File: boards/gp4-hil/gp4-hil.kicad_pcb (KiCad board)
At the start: 4 copper layers, 145 x 41 mm, 488 parts, among them J1 BEL_FUSE_0826-1G1T-23-F, J2 XILINX_JTAG, J3 XILINX_JTAG_ICESIDE, J4 XILINX_JTAG_ICESIDE, K1 CONN_3_PWROUT, P1 GPAK_ZIF, P2 2x10 HEADER, Q1 SSM6N58NU, Q11 SSM6N58NU, Q12 DMP2069UFY4, Q13 SSM6N58NU, Q14 SSM6N58NU, Q15 SSM6N58NU, Q16 SSM6N58NU, Q17 SSM6N58NU, Q18 SSM6N58NU, Q19 SSM6N58NU, Q20 SSM6N58NU, Q21 SSM6N58NU, Q22 DMP2069UFY4, U1 MIC2288-DFN, U10 AD9609, U11 DAC084S085, U12 DAC084S085, U13 DAC084S085, U14 DAC084S085, U15 TS3A4751, U16 TS3A4751, U17 TS3A4751, U18 TS3A4751, U19 TS3A4751, U2 XC7A100T-1FTG256C, U20 SIP32408, U21 SIP32408, U22 SIP32408, U23 SIP32408, U24 SIP32408, U25 TS3A4751, U26 TS3A4751, U27 TS3A4751, U28 TS3A4751, U29 TXB0104RUT, U3 LTC3374-QFN, U30 TXB0104RUT, U31 ADA4937-2, U32 SIP32408, U33 125 MHz, U34 INA199A2RSW, U35 INA199A2RSW, U36 INA199A2RSW, U4 SIP32408, U5 KSZ9031RN, U6 W25Q32FW, U7 25 MHz, U8 ADG726, U9 AD9609

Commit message: More JTAG/config stuff
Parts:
- C163, C164, C165, C166, C182, C24, R121, R124, R127, R128, R130, R131, R132, R135, R136, R137: moved to B.Cu
- TP22, TP23: footprint azonenberg_pcb:TESTPOINT_SMT_KEYSTONE_5016 -> azonenberg_pcb:TESTPOINT_SMT_0.5MM
- moved TP35 126.6 mm to (148.3, 111.0)
- moved R122 123.5 mm to (142.3, 97.0), turned to 270 degrees
- moved R123 122.3 mm to (143.7, 96.9), turned to 270 degrees
- moved R132 122.2 mm to (143.7, 97.0), turned to 270 degrees
- moved R130 113.2 mm to (138.3, 95.2)
- moved R134 113.1 mm to (145.5, 87.8), turned to 180 degrees
- moved C143 112.1 mm to (138.7, 92.3), turned to 90 degrees
- moved R133 110.7 mm to (142.3, 87.2), turned to 270 degrees
- moved U6 106.0 mm to (143.0, 92.2)
- moved R127 104.8 mm to (125.0, 97.2), turned to 180 degrees
- moved R128 102.6 mm to (125.0, 96.2), turned to 180 degrees
- moved R121 101.7 mm to (112.5, 107.7), turned to 270 degrees
- moved R125 99.3 mm to (125.8, 98.1), turned to 180 degrees
- moved R129 95.8 mm to (143.7, 87.2), turned to 90 degrees
- moved R131 94.7 mm to (142.3, 87.2), turned to 90 degrees
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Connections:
- U2 pad N9: /Ethernet + JTAG/VPP_EN -> /Ethernet + JTAG/JTAGA_OE
- U2 pad P6: /Ethernet + JTAG/JTAGB_OE -> /Ethernet + JTAG/VPP_EN
- U2 pad R10: /DUT/DUT_VDD2_EN -> /Ethernet + JTAG/JTAGA_TDO
- U2 pad R11: /Ethernet + JTAG/VDD1_3V3_EN -> /Ethernet + JTAG/JTAGA_TMS
- U2 pad R5: /Ethernet + JTAG/JTAGB_TMS -> /DUT/DUT_VDD2_EN
- U2 pad R6: /Ethernet + JTAG/JTAGB_TDO -> /Ethernet + JTAG/JTAGB_TDI
- U2 pad R7: /Ethernet + JTAG/JTAGB_TDI -> /Ethernet + JTAG/JTAGB_TCK
- U2 pad R8: /Ethernet + JTAG/JTAGA_TMS -> /Ethernet + JTAG/JTAGB_OE
- U2 pad T10: /Ethernet + JTAG/JTAGA_OE -> /Ethernet + JTAG/JTAGA_TCK
- U2 pad T5: /Ethernet + JTAG/JTAGB_TCK -> /Ethernet + JTAG/VDD1_3V3_EN
- U2 pad T7: /Ethernet + JTAG/JTAGA_TCK -> /Ethernet + JTAG/JTAGB_TDO
- U2 pad T8: /Ethernet + JTAG/JTAGA_TDO -> /Ethernet + JTAG/JTAGB_TMS
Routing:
- net /Analog IO/GND: track 328.0 -> 571.1 mm, vias 79 -> 95
- net /Analog IO/1V8: track 81.6 -> 191.3 mm, vias 18 -> 29
- net /FPGA support/JTAG_TMS: track 0.71 -> 57.6 mm
- net /FPGA support/JTAG_TCK: track 0.71 -> 55.9 mm, vias 1 -> 2
- net /FPGA support/JTAG_TDI: track 0.71 -> 52.3 mm, vias 1 -> 2
- net /FPGA support/JTAG_TDO: track 0.00 -> 47.3 mm
- net /FPGA support/FLASH_SCK: track 0.71 -> 42.9 mm, vias 1 -> 2
- net /FPGA support/FLASH_DQ3T: track 0.00 -> 31.1 mm, vias 0 -> 2
- net /FPGA support/FLASH_DQ0T: track 0.00 -> 26.6 mm, vias 0 -> 1
- net /FPGA support/FLASH_DQ2T: track 0.00 -> 18.4 mm
- net /FPGA support/FLASH_CS_NT: track 0.00 -> 18.2 mm, vias 0 -> 1
- net /FPGA support/FLASH_DQ1T: track 0.00 -> 17.4 mm, vias 0 -> 1
- net /Ethernet + JTAG/JTAGB_VCCAUX: track 0.00 -> 17.0 mm, vias 0 -> 1
- net /Ethernet + JTAG/JTAGA_OE: track 0.00 -> 16.2 mm, vias 0 -> 2
- net /Ethernet + JTAG/JTAGB_OE: track 0.71 -> 16.1 mm, vias 1 -> 0
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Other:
- board size 145 x 41 mm -> 145 x 60 mm
- board text added: "5V DC"
- board text added: "FPGA JTAG"
- board text added: "FPGA config"
- board text added: "GND"
- board text added: "GreenPak Toolchain Test v0.1 A. Zonenberg / 2016-05-26"
- board text added: "MASTER JTAG A"
- board text added: "MASTER JTAG B"
- board text removed: "Clocks"
- board text removed: "FPGA config straps"
- board text removed: "FPGA config/boot"
- board text removed: "JTAG"
- board text removed: "Power inlet"

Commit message: Began routing level shifters
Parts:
- C116, C117, C118, C119, C120, C121, C123, C124, C140, C172, F1, L8, Q22, R103, R117, R118, R120, R177: moved to B.Cu
- moved TP36 148.7 mm to (53.3, 114.8)
- moved U23 145.8 mm to (97.8, 108.8), turned to 270 degrees
- moved Q1 143.9 mm to (140.7, 42.7), turned to 90 degrees
- moved R81 143.3 mm to (143.7, 41.6)
- moved U22 141.9 mm to (97.8, 105.5), turned to 270 degrees
- moved C140 138.7 mm to (97.9, 105.7), turned to 180 degrees
- moved C58 138.4 mm to (148.7, 44.1)
- moved C61 137.6 mm to (151.9, 44.0)
- moved C62 137.6 mm to (156.9, 44.2)
- moved D1 137.4 mm to (143.6, 44.2)
- moved C57 137.2 mm to (152.2, 41.4)
- moved C59 137.2 mm to (149.1, 41.5)
- moved C60 137.2 mm to (156.9, 41.6)
- moved R118 131.9 mm to (98.5, 107.7), turned to 90 degrees
- moved R117 126.3 mm to (100.0, 108.0), turned to 270 degrees
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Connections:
- U2 pad A2: /Digital IO/GPIO19_DEN -> (no net)
- U2 pad B2: /Digital IO/GPIO18_DEN -> (no net)
- U2 pad C1: /Digital IO/GPIO20_DEN -> (no net)
- U2 pad C2: /Digital IO/GPIO17_DEN -> (no net)
- U2 pad C3: /Digital IO/GPIO16_DEN -> (no net)
- U2 pad C6: /Digital IO/GPIO13_DEN -> (no net)
- U2 pad C7: /Digital IO/GPIO12_DEN -> (no net)
- U2 pad D5: /Digital IO/GPIO15_DEN -> (no net)
- U2 pad D6: /Digital IO/GPIO14_DEN -> (no net)
- U2 pad G11: (no net) -> /Analog IO/ADC_A_MODE
- U2 pad G15: (no net) -> /Analog IO/DAC_SCLK
- U2 pad J15: /Analog IO/DAC_SCLK -> (no net)
- U2 pad J16: /Analog IO/ADC_A_MODE -> (no net)
- U2 pad L14: /Ethernet + JTAG/VDD2_2V5_EN -> /Ethernet + JTAG/VPP_EN
- U2 pad M14: /Ethernet + JTAG/VDD2_3V3_EN -> (no net)
- U2 pad M15: /Ethernet + JTAG/VDD2_1V8_EN -> /Ethernet + JTAG/VDD1_3V3_EN
- U2 pad M5: (no net) -> /Digital IO/GPIO13_DEN
- U2 pad N1: /Digital IO/GPIO18_DIO -> /Digital IO/GPIO15_DEN
- U2 pad N2: /Digital IO/GPIO17_DIO -> /Digital IO/GPIO12_DEN
- U2 pad N3: /Digital IO/GPIO16_DIO -> /Digital IO/GPIO20_DIO
- U2 pad N4: (no net) -> /Digital IO/GPIO14_DEN
- U2 pad N6: (no net) -> /DUT/DUT_VDD2_EN
- U2 pad P1: /Digital IO/GPIO19_DIO -> /Digital IO/GPIO18_DEN
- U2 pad P3: (no net) -> /Digital IO/GPIO18_DIO
- U2 pad P4: /Digital IO/GPIO20_DIO -> /Digital IO/GPIO19_DIO
- U2 pad P6: /Ethernet + JTAG/VPP_EN -> /Ethernet + JTAG/VDD2_2V5_EN
- U2 pad R1: (no net) -> /Digital IO/GPIO17_DEN
- U2 pad R2: (no net) -> /Digital IO/GPIO17_DIO
- U2 pad R3: (no net) -> /Digital IO/GPIO20_DEN
- U2 pad R5: /DUT/DUT_VDD2_EN -> /Ethernet + JTAG/VDD2_3V3_EN
- U2 pad T2: (no net) -> /Digital IO/GPIO16_DIO
- U2 pad T3: (no net) -> /Digital IO/GPIO16_DEN
- U2 pad T4: (no net) -> /Digital IO/GPIO19_DEN
- U2 pad T5: /Ethernet + JTAG/VDD1_3V3_EN -> /Ethernet + JTAG/VDD2_1V8_EN
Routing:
- net /Analog IO/GND: track 571.1 -> 779.1 mm, vias 95 -> 140
- net /Analog IO/2V5: track 39.5 -> 186.9 mm, vias 9 -> 18
- net /Analog IO/1V8: track 191.3 -> 291.6 mm, vias 29 -> 40
- net /Power supply/5V0: track 1.15 -> 92.0 mm, vias 0 -> 24
- net /FPGA support/1V0: track 42.0 -> 113.0 mm, vias 11 -> 19
- net /Analog IO/3V3: track 0.00 -> 59.7 mm, vias 0 -> 8
- net /FPGA support/PSU_PGOOD: track 0.71 -> 58.4 mm, vias 1 -> 2
- net /Power supply/1V0_VSENSE: track 0.00 -> 51.8 mm, vias 0 -> 1
- net /Ethernet + JTAG/1V2: track 25.9 -> 62.2 mm, vias 7 -> 13
- net /Power supply/FB_1V8: track 0.00 -> 18.9 mm, vias 0 -> 2
- net /Digital IO/GPIO19_DEN: track 0.00 -> 18.7 mm
- net /Digital IO/GPIO19_DIO: track 0.71 -> 17.3 mm, vias 1 -> 2
- net /Ethernet + JTAG/VDD2_2V5_EN: track 0.71 -> 17.0 mm, vias 1 -> 0
- net /Digital IO/GPIO18_DIO: track 0.71 -> 16.9 mm, vias 1 -> 2
- net /Digital IO/GPIO16_DEN: track 0.71 -> 16.3 mm, vias 1 -> 0
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- added copper zone on In2.Cu, net /Analog IO/1V8
- added copper zone on In2.Cu, net /Analog IO/2V5
- added copper zone on In2.Cu, net /Ethernet + JTAG/1V2
- added copper zone on In2.Cu, net /Ethernet + JTAG/A1V2_ETH
- added copper zone on In2.Cu, net /Ethernet + JTAG/A2V5_ETH
- added copper zone on In2.Cu, net /FPGA support/1V0
- added copper zone on In2.Cu, net /Power supply/5V0
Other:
- board text added: "1V0"
- board text added: "1V2"
- board text added: "1V8"
- board text added: "2V5"
- board text added: "3V3"
- board text added: "PGOOD"
- board text added: "VTEMP"
- board text removed: "Digital isolation switching"
- board text removed: "FPGA config"
- board text removed: "Main PSU"

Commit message: Continue work on digital I/O routing
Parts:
- C58, C59, R184, R185, R186: moved to B.Cu
- moved C176 176.9 mm to (21.8, 140.8)
- moved C178 176.9 mm to (32.9, 145.2)
- moved R178 176.9 mm to (29.0, 140.8)
- moved U34 176.9 mm to (29.0, 146.2)
- moved U35 176.9 mm to (19.0, 146.2)
- moved U36 176.9 mm to (24.8, 146.4)
- moved D20 137.4 mm to (77.3, 48.0)
- moved R113 137.4 mm to (80.8, 57.2)
- moved C129 137.4 mm to (94.8, 48.7)
- moved C130 137.4 mm to (88.7, 53.9)
- moved Q11 137.4 mm to (66.5, 46.8)
- moved R114 137.4 mm to (71.9, 48.5)
- moved TP30 137.4 mm to (62.2, 52.5)
- moved U1 137.4 mm to (83.0, 47.5)
- moved L12 137.4 mm to (88.8, 48.7)
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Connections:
- U2 pad L4: /Digital IO/GPIO12_DIO -> /Digital IO/GPIO20_DIO
- U2 pad M1: /Digital IO/GPIO15_DIO -> /Digital IO/GPIO13_DIO
- U2 pad M2: /Digital IO/GPIO14_DIO -> /Digital IO/GPIO12_DIO
- U2 pad M4: /Digital IO/GPIO13_DIO -> /Digital IO/GPIO14_DEN
- U2 pad N1: /Digital IO/GPIO15_DEN -> /Digital IO/GPIO12_DEN
- U2 pad N2: /Digital IO/GPIO12_DEN -> /Digital IO/GPIO15_DEN
- U2 pad N3: /Digital IO/GPIO20_DIO -> /Digital IO/GPIO14_DIO
- U2 pad N4: /Digital IO/GPIO14_DEN -> /Digital IO/GPIO15_DIO
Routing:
- net /Analog IO/DUT_GPIO19: track 2.25 -> 30.4 mm, vias 0 -> 1
- net /Analog IO/DUT_GPIO18: track 2.30 -> 29.4 mm, vias 0 -> 1
- net /Analog IO/DUT_GPIO17: track 6.99 -> 32.5 mm, vias 1 -> 3
- net /Analog IO/DUT_GPIO16: track 6.49 -> 31.8 mm, vias 1 -> 3
- net /Analog IO/DUT_GPIO13: track 0.00 -> 24.0 mm, vias 0 -> 3
- net /Analog IO/DUT_GPIO12: track 0.00 -> 22.3 mm, vias 0 -> 3
- net /Analog IO/DUT_GPIO15: track 0.00 -> 21.1 mm, vias 0 -> 1
- net /Analog IO/DUT_GPIO14: track 0.00 -> 19.9 mm, vias 0 -> 1
- net /Digital IO/GPIO14_DIO: track 0.00 -> 19.2 mm, vias 0 -> 2
- net /Digital IO/GPIO13_DEN: track 0.00 -> 18.1 mm, vias 0 -> 2
- net /Digital IO/GPIO15_DIO: track 0.00 -> 18.1 mm, vias 0 -> 2
- net /Digital IO/GPIO14_DEN: track 0.71 -> 18.8 mm, vias 1 -> 2
- net /Analog IO/DUT_VDD1: track 25.6 -> 42.4 mm, vias 7 -> 11
- net /Digital IO/GPIO15_DEN: track 0.00 -> 15.0 mm
- net /Analog IO/DUT_GPIO10: track 0.00 -> 13.6 mm, vias 0 -> 1
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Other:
- board text added: "VDD2 3V3 2V5 1V8"
- board text removed: "PSU test points"

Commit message: Continued general PCB layout
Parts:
- R178, U35: moved to B.Cu
- moved TP15 171.9 mm to (38.0, 71.0)
- moved TP13 155.9 mm to (26.0, 71.0)
- moved TP16 144.6 mm to (44.0, 71.0)
- moved TP12 142.0 mm to (26.0, 114.0)
- moved TP17 138.5 mm to (50.0, 71.0)
- moved TP8 137.2 mm to (50.0, 114.0)
- moved TP21 136.6 mm to (74.0, 71.0)
- moved TP11 130.7 mm to (32.0, 114.0)
- moved TP14 129.8 mm to (32.0, 71.0)
- moved P2 127.3 mm to (24.2, 92.5), turned to 270 degrees
- moved TP18 127.0 mm to (56.0, 71.0)
- moved TP7 125.5 mm to (56.0, 114.0)
- moved TP19 121.4 mm to (62.0, 71.0)
- moved TP10 116.6 mm to (38.0, 114.0)
- moved TP3 114.9 mm to (86.0, 71.0)
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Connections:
- U2 pad A3: /Digital IO/GPIO10_DEN -> (no net)
- U2 pad A4: /Digital IO/GPIO8_DEN -> (no net)
- U2 pad A5: /Digital IO/GPIO7_DEN -> /Analog IO/GPIO17_AEN
- U2 pad A7: /Digital IO/GPIO4_DEN -> /Analog IO/GPIO13_AEN
- U2 pad B4: /Digital IO/GPIO9_DEN -> (no net)
- U2 pad B5: /Digital IO/GPIO6_DEN -> /Analog IO/GPIO9_AEN
- U2 pad B6: /Digital IO/GPIO5_DEN -> /Analog IO/GPIO6_AEN
- U2 pad B7: /Digital IO/GPIO3_DEN -> /Analog IO/GPIO10_AEN
- U2 pad C4: /Digital IO/GPIO8_DIO -> (no net)
- U2 pad D1: /Digital IO/GPIO4_DIO -> /Digital IO/GPIO5_DEN
- U2 pad D3: /Digital IO/GPIO6_DIO -> (no net)
- U2 pad D4: /Digital IO/GPIO7_DIO -> (no net)
- U2 pad E1: /Analog IO/GPIO6_AEN -> /Digital IO/GPIO4_DIO
- U2 pad E2: /Digital IO/GPIO3_DIO -> /Analog IO/GPIO5_AEN
- U2 pad E3: /Digital IO/GPIO5_DIO -> /Digital IO/GPIO4_DEN
- U2 pad E5: /Digital IO/GPIO10_DIO -> /Analog IO/GPIO15_AEN
- U2 pad F2: /Analog IO/GPIO5_AEN -> /Digital IO/GPIO3_DIO
- U2 pad G1: /Analog IO/GPIO10_AEN -> /Digital IO/GPIO3_DEN
- U2 pad G2: /Analog IO/GPIO9_AEN -> /Digital IO/GPIO6_DEN
- U2 pad H1: (no net) -> /Digital IO/GPIO9_DEN
- U2 pad H2: /Analog IO/GPIO17_AEN -> /Digital IO/GPIO8_DEN
- U2 pad H3: (no net) -> /Digital IO/GPIO5_DIO
- U2 pad H4: /Analog IO/GPIO13_AEN -> /Digital IO/GPIO6_DIO
- U2 pad J1: (no net) -> /Digital IO/GPIO8_DIO
- U2 pad J4: /Analog IO/GPIO15_AEN -> /Digital IO/GPIO10_DIO
- U2 pad K1: (no net) -> /Digital IO/GPIO7_DIO
- U2 pad K2: (no net) -> /Digital IO/GPIO7_DEN
- U2 pad L2: (no net) -> /Digital IO/GPIO10_DEN
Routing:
- net /Analog IO/DUT_GPIO8: track 0.00 -> 136.5 mm, vias 0 -> 1
- net /Analog IO/DUT_GPIO10: track 13.6 -> 146.3 mm
- net /Analog IO/DUT_GPIO7: track 0.00 -> 130.8 mm, vias 0 -> 1
- net /Analog IO/DUT_GPIO12: track 22.3 -> 152.4 mm
- net /Analog IO/DUT_GPIO6: track 0.00 -> 128.1 mm, vias 0 -> 3
- net /Analog IO/DUT_GPIO9: track 10.3 -> 138.1 mm
- net /Analog IO/DUT_GPIO13: track 24.0 -> 150.9 mm
- net /Analog IO/DUT_GPIO4: track 0.00 -> 123.5 mm, vias 0 -> 3
- net /Analog IO/DUT_GPIO5: track 0.00 -> 121.7 mm, vias 0 -> 3
- net /Analog IO/DUT_GPIO14: track 19.9 -> 136.1 mm, vias 1 -> 3
- net /Analog IO/DUT_GPIO15: track 21.1 -> 137.3 mm, vias 1 -> 3
- net /Analog IO/DUT_GPIO3: track 0.00 -> 111.1 mm, vias 0 -> 3
- net /Analog IO/DUT_GPIO16: track 31.8 -> 136.2 mm
- net /Analog IO/DUT_GPIO17: track 32.5 -> 133.4 mm
- net /Analog IO/DUT_GPIO18: track 29.4 -> 122.6 mm, vias 1 -> 3
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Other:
- board size 145 x 60 mm -> 160 x 60 mm
- board text added: "CLK"
- board text added: "CS_N"
- board text added: "DQ"
- board text added: "GreenPak Toolchain Test v0.1 A. Zonenberg / 2016-05-30"
- board text added: "IO10"
- board text added: "IO12"
- board text added: "IO13"
- board text added: "IO14"
- board text added: "IO15"
- board text added: "IO16"
- board text added: "IO17"
- board text added: "IO18"
- board text added: "IO19"
- board text added: "IO2"
- board text added: "IO20"
- board text added: "IO3"
- board text added: "IO4"
- board text added: "IO5"
- board text added: "IO6"
- board text added: "IO7"
- board text added: "IO8"
- board text added: "IO9"
- board text added: "MODE"
- board text added: "RST_N"
- board text added: "R~W"
- board text added: "VDD1"
- board text added: "VDD2"
- board text added: "VPP"
- board text removed: "GreenPak Toolchain Test v0.1 A. Zonenberg / 2016-05-26"

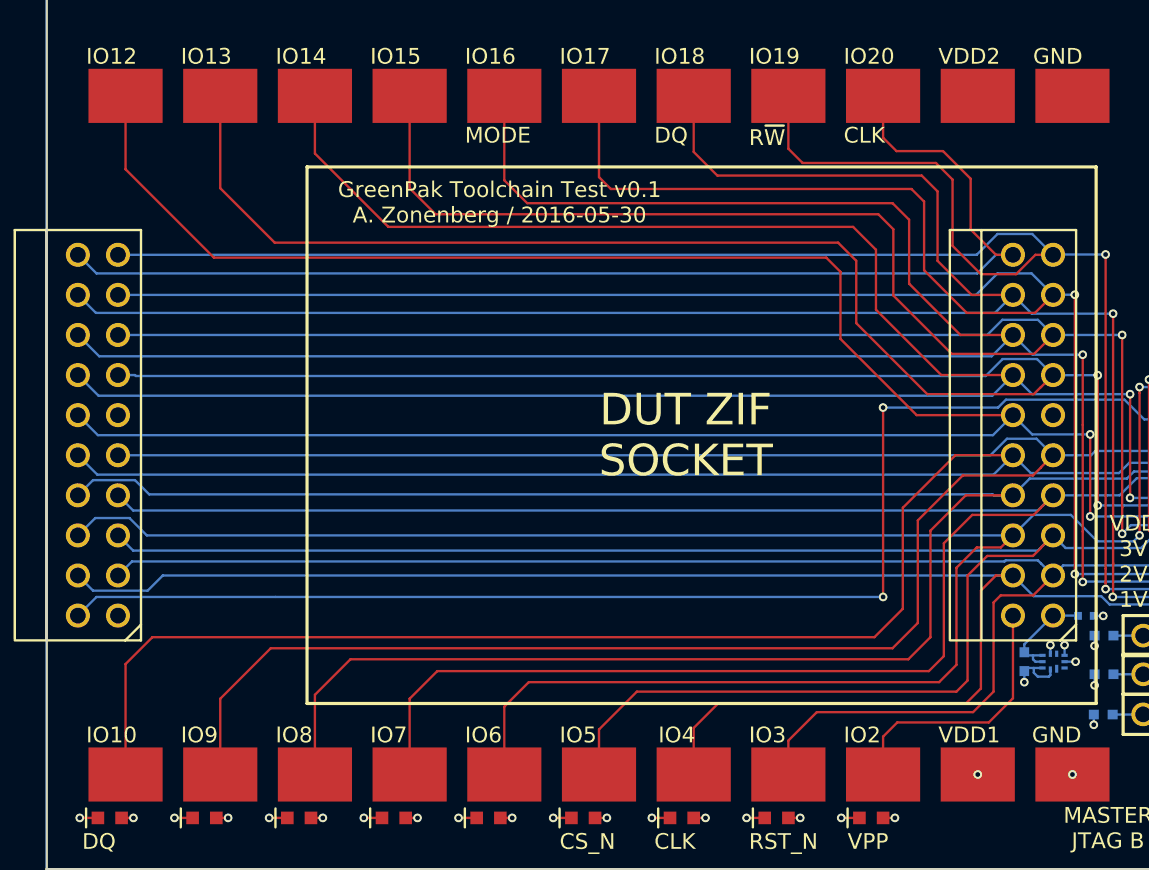
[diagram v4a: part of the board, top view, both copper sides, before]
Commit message: Routing cleanup on test pads for DUT
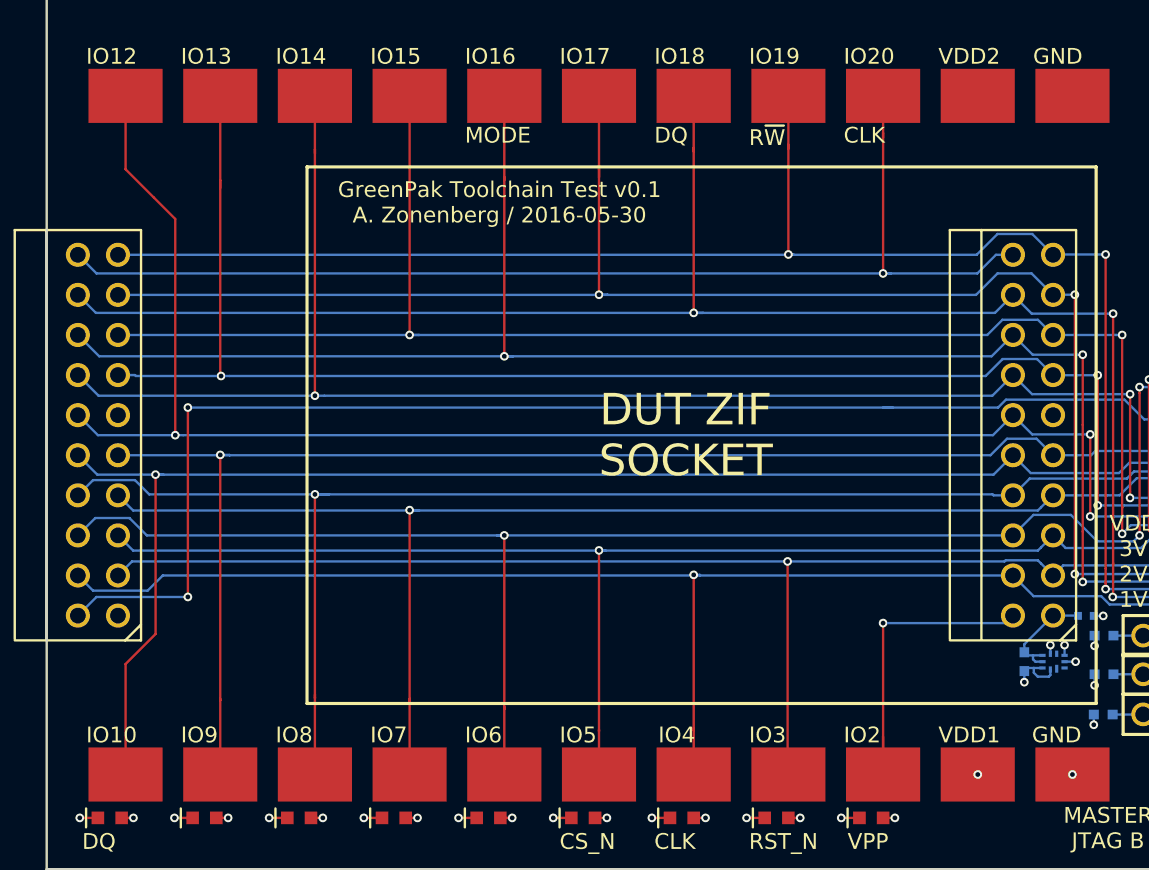
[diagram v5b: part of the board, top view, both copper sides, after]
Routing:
- net /Analog IO/DUT_GPIO10: track 146.3 -> 94.1 mm, vias 1 -> 2
- net /Analog IO/DUT_GPIO13: track 150.9 -> 102.4 mm, vias 3 -> 4
- net /Analog IO/DUT_GPIO12: track 152.4 -> 105.4 mm, vias 3 -> 4
- net /Analog IO/DUT_GPIO9: track 138.1 -> 91.3 mm, vias 1 -> 2
- net /Analog IO/DUT_GPIO8: track 136.5 -> 96.9 mm, vias 1 -> 2
- net /Analog IO/DUT_GPIO15: track 137.3 -> 99.3 mm, vias 3 -> 4
- net /Analog IO/DUT_GPIO7: track 130.8 -> 93.2 mm, vias 1 -> 2
- net /Analog IO/DUT_GPIO14: track 136.1 -> 99.4 mm, vias 3 -> 4
- net /Analog IO/DUT_GPIO6: track 128.1 -> 99.3 mm, vias 3 -> 4
- net /Analog IO/DUT_GPIO17: track 133.4 -> 106.6 mm, vias 3 -> 4
- net /Analog IO/DUT_GPIO16: track 136.2 -> 109.5 mm, vias 3 -> 4
- net /Analog IO/DUT_GPIO5: track 121.7 -> 95.8 mm, vias 3 -> 4
- net /Analog IO/DUT_GPIO4: track 123.5 -> 106.0 mm, vias 3 -> 4
- net /Analog IO/DUT_GPIO19: track 118.2 -> 102.5 mm, vias 3 -> 4
- net /Analog IO/DUT_GPIO18: track 122.6 -> 107.1 mm, vias 3 -> 4
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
